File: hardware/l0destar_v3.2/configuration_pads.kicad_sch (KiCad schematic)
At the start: 5 parts

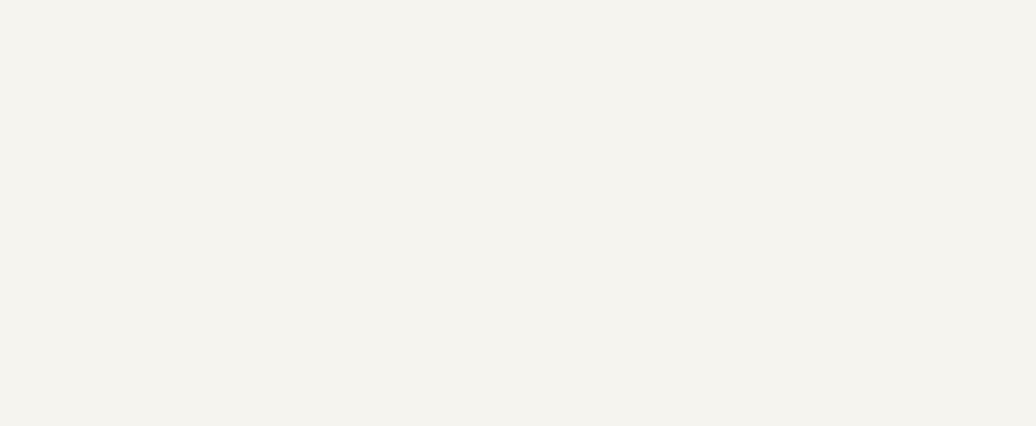
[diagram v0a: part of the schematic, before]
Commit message: update sheet annotations
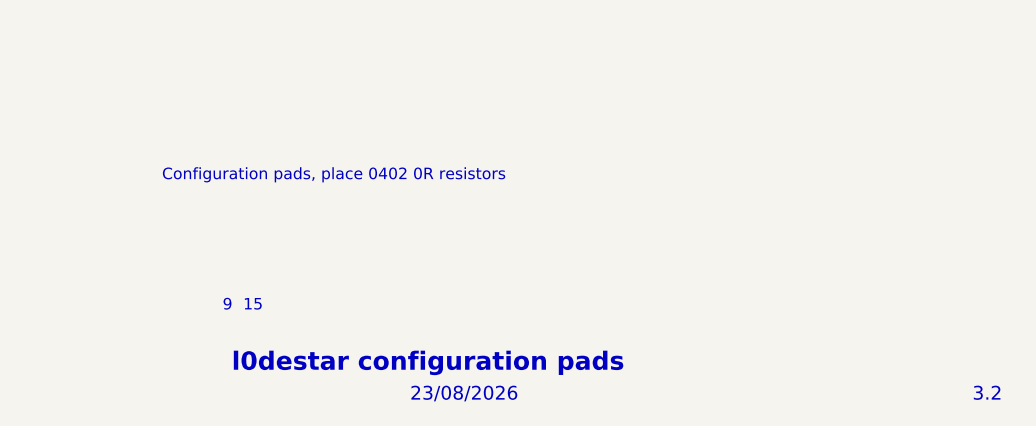
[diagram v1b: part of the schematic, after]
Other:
- note added: "15"
- note added: "23/08/2026"
- note added: "3.2"
- note added: "9"
- note added: "Configuration pads, place 0402 0R resistors"
- note added: "l0destar configuration pads"
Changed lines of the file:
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@@
+		)
+	)
+	(text "9"
+		(exclude_from_sim no)
+		(at 185.801 183.388 0)
+		(effects
+			(font
+				(size 1.27 1.27)
+			)
+			(justify left)
+		)
+	)
+	(text "Configuration pads, place 0402 0R resistors"
+		(exclude_from_sim no)
+		(at 179.07 168.91 0)
+		(effects
+			(font
+				(size 1.27 1.27)
+			)
+			(justify left)
+		)
+	)
+	(text "15"
+		(exclude_from_sim no)
+		(at 188.087 183.388 0)
+		(effects
+			(font
+				(size 1.27 1.27)
+			)
+			(justify left)
+		)
+	)
+	(text "l0destar configuration pads"
+		(exclude_from_sim no)
+		(at 186.817 189.738 0)
+		(effects
+			(font
+				(face "KiCad Font")
+				(size 2.032 2.032)
+				(thickness 0.4064)
+				(bold yes)
+			)
+			(justify left)
+		)
+	)
+	(text "23/08/2026"
+		(exclude_from_sim no)
+		(at 206.629 193.294 0)
+		(effects
+			(font
+				(face "KiCad Font")
+				(size 1.524 1.524)
+				(thickness 0.1905)
+			)
+			(justify left)
+		)
+	)
+	(text "3.2"
+		(exclude_from_sim no)
+		(at 269.113 193.294 0)
+		(effects
+			(font
+				(face "KiCad Font")
+				(size 1.524 1.524)
+				(thickness 0.1905)
+			)
+			(justify left)
 		)
 	)
